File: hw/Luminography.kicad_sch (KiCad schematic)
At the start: 109 parts, among them J1 USB_C_Receptacle_PowerOnly_6P, J2 Conn_01x04, Q1 MMBT3904, Q2 2N7002, SW1 SW_Push, U1 LTC4054ES5-4.2, U100 BH1750FVI-TR, U101 BH1750FVI-TR, U102 BH1750FVI-TR, U103 BH1750FVI-TR, U104 BH1750FVI-TR, U105 BH1750FVI-TR, U106 BH1750FVI-TR, U107 BH1750FVI-TR, U108 BH1750FVI-TR, U109 BH1750FVI-TR, U110 BH1750FVI-TR, U111 BH1750FVI-TR, U112 BH1750FVI-TR, U113 BH1750FVI-TR, U114 BH1750FVI-TR, U115 BH1750FVI-TR, U116 BH1750FVI-TR, U117 BH1750FVI-TR, U118 BH1750FVI-TR, U119 BH1750FVI-TR, U120 BH1750FVI-TR, U121 BH1750FVI-TR, U122 BH1750FVI-TR, U123 BH1750FVI-TR, U2 XS3A1T3157GMX, U3 SPX3819M5-L-3-3, U4 MAX17048G+T10, U5 STM32G030K6Tx, U6 ZJY128R-IG01, U7 BMI270, U8 MMC5603NJ, U9 MAX98357AETE+, X1 12.288MHz

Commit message: Finish sensor array layout
そんなこと今更叶わない
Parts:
- C1, C10, C100, C101, C102, C103, C104, C105, C106, C107, C108, C109, C11, C110, C111, C112, C113, C114, C115, C116, C117, C118, C119, C12, C120, C121, C122, C123, C13, C14, C15, C2, C3, C4, C5, C6, C7, C8, C9: footprint Resistor_SMD:R_0402_1005Metric -> Capacitor_SMD:C_0402_1005Metric
- D1: footprint Resistor_SMD:R_0402_1005Metric -> Diode_SMD:D_SMB
- D2, D3: footprint Resistor_SMD:R_0402_1005Metric -> LED_SMD:LED_0603_1608Metric
- J1: footprint Resistor_SMD:R_0402_1005Metric -> Luminography_footprints:USB_C_Receptacle
- J2: footprint Resistor_SMD:R_0402_1005Metric -> Luminography_footprints:TestPoints_1x04_P2.0
- L1: footprint Resistor_SMD:R_0402_1005Metric -> Inductor_SMD:L_0402_1005Metric
- LS1: footprint Resistor_SMD:R_0402_1005Metric -> Luminography_footprints:Pads_1x02_P2.5
- Q1, Q2: footprint Resistor_SMD:R_0402_1005Metric -> Package_TO_SOT_SMD:SOT-23
- renumbered R101 to R102, R102 to R104, R103 to R106, R104 to R108, R105 to R110, R106 to R112, R107 to R114, R108 to R116, R109 to R118, R110 to R120, R111 to R122

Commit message: 🚧 Layout WIP
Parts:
- removed D3: White, LED_SMD:LED_0603_1608Metric, symbol Device:LED
- removed R13: 7.5k, Resistor_SMD:R_0402_1005Metric, symbol Device:R
- added C11: 100n, Capacitor_SMD:C_0402_1005Metric, symbol Device:C
- added U7: W25Q16JVUXIQ, W25Q16JVUXIQ:SON50P300X200X60-9N, symbol W25Q16JVUXIQ:W25Q16JVUXIQ
- renumbered C15 to C10, C9 to C12, C10 to C13, C11 to C14, C12 to C15, C13 to C16, C14 to C9, U9 to U10, U7 to U8, U8 to U9
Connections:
- net ACT_LED is gone; now on net I2Cx_SCL: U5.21 (PA10/NC)
- net GND: now also C11.1, U7.4 (GND), U7.9 (EP)
- net I2Cx_SCL: no longer U5.19 (PA9/NC)
- net PWR_LATCH: now also U5.22 (PA11/PA9)
- net SPI_MOSI: now also U7.5 (DI_(IO0))
- net SPI_SCK: now also U7.6 (CLK)
- net VDD: now also C11.2, U7.8 (VCC)
- net FLASH_CS: now reaches U5.20 (PC6)
- net FLASH_CS: now also U7.1 (~{CS})
- net BTN_INTR renamed BTNA_INTR
- new net SPI_MISO: U5.19 (PA9/NC), U7.2 (DO_(IO1))
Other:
- note added: "PA9 AF4 SPI2_MISO"
- moved on the sheet: R11

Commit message: 🚧 Routing WIP
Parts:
- removed Q1: MMBT3904, Package_TO_SOT_SMD:SOT-23, symbol Transistor_BJT:MMBT3904
- removed R5: 1M, Resistor_SMD:R_0402_1005Metric, symbol Device:R
- added R12: 1k, Resistor_SMD:R_0402_1005Metric, symbol Device:R
- added R6: 1M, Resistor_SMD:R_0402_1005Metric, symbol Device:R
- added SW2: SW_Push, Button_Switch_SMD:SW_SPST_TL3342, symbol Switch:SW_Push
- R5: renamed from R6; value 30k -> 1M
- renumbered Q2 to Q1, R12 to R13
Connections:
- net BTNA_INTR: now also R5.1, SW1.2, U2.3 (Y1), U5.22 (PA11/PA9); no longer R5.2
- net GND: now also R5.2, U8.1 (SDO), R6.2
- net I2Cx_SCL: now also U8.13 (SCX)
- net I2Cx_SDA_00: now also U8.14 (SDX)
- net LCD_CS: now also U5.1 (PB9); no longer U5.30 (PB6)
- net LCD_RSTN: now also U5.30 (PB6); no longer U5.1 (PB9)
- net PWR_LATCH: now also U5.3 (PC15); no longer U5.22 (PA11/PA9)
- net SPI_MOSI: no longer U8.14 (SDX)
- net SPI_SCK: no longer U8.13 (SCX)
- net SWDIO: now also R12.2; no longer U5.24 (PA13)
- net VDD: now also U8.12 (CSB), SW2.1; no longer R5.1
- removed net BMI_CS: U5.3 (PC15), U8.12 (CSB)
- new net BTNB_INTR: R12.1, R6.1, SW2.2, U5.24 (PA13)
- no-connect marks 16 -> 15
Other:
- note added: "Do not press when connected to a debug probe"
- note added: "Requires 5 V tolerance"
- moved on the sheet: C10, C3, C4, R13, R5, U3

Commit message: Board design almost done, do later
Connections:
- net I2Cx_SDA_00: now also U5.14 (PA7); no longer U5.7 (PA0)
- net I2Cx_SDA_01: now also U5.15 (PB0); no longer U5.8 (PA1)
- net I2Cx_SDA_02: now also U5.16 (PB1); no longer U5.9 (PA2)
- net I2Cx_SDA_03: now also U5.17 (PB2); no longer U5.10 (PA3)
- net I2Cx_SDA_04: now also U5.18 (PA8); no longer U5.11 (PA4)
- net I2Cx_SDA_05: now also U5.7 (PA0); no longer U5.12 (PA5)
- net I2Cx_SDA_06: now also U5.8 (PA1); no longer U5.13 (PA6)
- net I2Cx_SDA_07: now also U5.9 (PA2); no longer U5.14 (PA7)
- net I2Cx_SDA_08: now also U5.10 (PA3); no longer U5.15 (PB0)
- net I2Cx_SDA_09: now also U5.11 (PA4); no longer U5.16 (PB1)
- net I2Cx_SDA_10: now also U5.12 (PA5); no longer U5.17 (PB2)
- net I2Cx_SDA_11: now also U5.13 (PA6); no longer U5.18 (PA8)
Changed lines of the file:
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@@
     )
   )
-  (global_label "I2Cx_SDA_02" (shape bidirectional) (at 100.33 88.9 0) (fields_autoplaced)
+  (global_label "I2Cx_SDA_07" (shape bidirectional) (at 100.33 88.9 0) (fields_autoplaced)
     (effects (font (size 1.27 1.27)) (justify left))
     (property "Intersheetrefs" "${INTERSHEET_REFS}" (at 116.4612 88.9 0)
@@
     )
   )
-  (global_label "I2Cx_SDA_07" (shape bidirectional) (at 100.33 101.6 0) (fields_autoplaced)
+  (global_label "I2Cx_SDA_00" (shape bidirectional) (at 100.33 101.6 0) (fields_autoplaced)
     (effects (font (size 1.27 1.27)) (justify left))
     (property "Intersheetrefs" "${INTERSHEET_REFS}" (at 116.4612 101.6 0)
@@
     )
   )
-  (global_label "I2Cx_SDA_03" (shape bidirectional) (at 100.33 91.44 0) (fields_autoplaced)
+  (global_label "I2Cx_SDA_08" (shape bidirectional) (at 100.33 91.44 0) (fields_autoplaced)
     (effects (font (size 1.27 1.27)) (justify left))
     (property "Intersheetrefs" "${INTERSHEET_REFS}" (at 116.4612 91.44 0)
@@
     )
   )
-  (global_label "I2Cx_SDA_08" (shape bidirectional) (at 72.39 99.06 180) (fields_autoplaced)
+  (global_label "I2Cx_SDA_01" (shape bidirectional) (at 72.39 99.06 180) (fields_autoplaced)
     (effects (font (size 1.27 1.27)) (justify right))
     (property "Intersheetrefs" "${INTERSHEET_REFS}" (at 56.2588 99.06 0)
@@
     )
   )
-  (global_label "I2Cx_SDA_10" (shape bidirectional) (at 72.39 104.14 180) (fields_autoplaced)
+  (global_label "I2Cx_SDA_03" (shape bidirectional) (at 72.39 104.14 180) (fields_autoplaced)
     (effects (font (size 1.27 1.27)) (justify right))
     (property "Intersheetrefs" "${INTERSHEET_REFS}" (at 56.2588 104.14 0)
@@
     )
   )
-  (global_label "I2Cx_SDA_04" (shape bidirectional) (at 100.33 93.98 0) (fields_autoplaced)
+  (global_label "I2Cx_SDA_09" (shape bidirectional) (at 100.33 93.98 0) (fields_autoplaced)
     (effects (font (size 1.27 1.27)) (justify left))
     (property "Intersheetrefs" "${INTERSHEET_REFS}" (at 116.4612 93.98 0)
@@
     )
   )
-  (global_label "I2Cx_SDA_01" (shape bidirectional) (at 100.33 86.36 0) (fields_autoplaced)
+  (global_label "I2Cx_SDA_06" (shape bidirectional) (at 100.33 86.36 0) (fields_autoplaced)
     (effects (font (size 1.27 1.27)) (justify left))
     (property "Intersheetrefs" "${INTERSHEET_REFS}" (at 116.4612 86.36 0)
@@
     )
   )
-  (global_label "I2Cx_SDA_11" (shape bidirectional) (at 100.33 104.14 0) (fields_autoplaced)
+  (global_label "I2Cx_SDA_04" (shape bidirectional) (at 100.33 104.14 0) (fields_autoplaced)
     (effects (font (size 1.27 1.27)) (justify left))
     (property "Intersheetrefs" "${INTERSHEET_REFS}" (at 116.4612 104.14 0)
@@
     )
   )
-  (global_label "I2Cx_SDA_00" (shape bidirectional) (at 100.33 83.82 0) (fields_autoplaced)
+  (global_label "I2Cx_SDA_05" (shape bidirectional) (at 100.33 83.82 0) (fields_autoplaced)
     (effects (font (size 1.27 1.27)) (justify left))
     (property "Intersheetrefs" "${INTERSHEET_REFS}" (at 116.4612 83.82 0)
@@
     )
   )
-  (global_label "I2Cx_SDA_09" (shape bidirectional) (at 72.39 101.6 180) (fields_autoplaced)
+  (global_label "I2Cx_SDA_02" (shape bidirectional) (at 72.39 101.6 180) (fields_autoplaced)
     (effects (font (size 1.27 1.27)) (justify right))
     (property "Intersheetrefs" "${INTERSHEET_REFS}" (at 56.2588 101.6 0)
@@
     )
   )
-  (global_label "I2Cx_SDA_06" (shape bidirectional) (at 100.33 99.06 0) (fields_autoplaced)
+  (global_label "I2Cx_SDA_11" (shape bidirectional) (at 100.33 99.06 0) (fields_autoplaced)
     (effects (font (size 1.27 1.27)) (justify left))
     (property "Intersheetrefs" "${INTERSHEET_REFS}" (at 116.4612 99.06 0)
@@
     )
   )
-  (global_label "I2Cx_SDA_05" (shape bidirectional) (at 100.33 96.52 0) (fields_autoplaced)
+  (global_label "I2Cx_SDA_10" (shape bidirectional) (at 100.33 96.52 0) (fields_autoplaced)
     (effects (font (size 1.27 1.27)) (justify left))
     (property "Intersheetrefs" "${INTERSHEET_REFS}" (at 116.4612 96.52 0)

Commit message: Finish routing
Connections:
- net I2Cx_SDA_00: no longer U4.8 (SDA), U8.14 (SDX)
- net I2Cx_SDA_04: now also U8.14 (SDX)
- net I2Cx_SDA_06: now also U4.8 (SDA)
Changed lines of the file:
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@@
     )
   )
-  (global_label "I2Cx_SDA_00" (shape bidirectional) (at 335.28 31.115 0) (fields_autoplaced)
+  (global_label "I2Cx_SDA_06" (shape bidirectional) (at 335.28 31.115 0) (fields_autoplaced)
     (effects (font (size 1.27 1.27)) (justify left))
     (property "Intersheetrefs" "${INTERSHEET_REFS}" (at 351.4112 31.115 0)
@@
     )
   )
-  (global_label "I2Cx_SDA_00" (shape bidirectional) (at 151.765 149.86 90) (fields_autoplaced)
+  (global_label "I2Cx_SDA_04" (shape bidirectional) (at 151.765 149.86 90) (fields_autoplaced)
     (effects (font (size 1.27 1.27)) (justify left))
     (property "Intersheetrefs" "${INTERSHEET_REFS}" (at 151.765 133.7288 90)

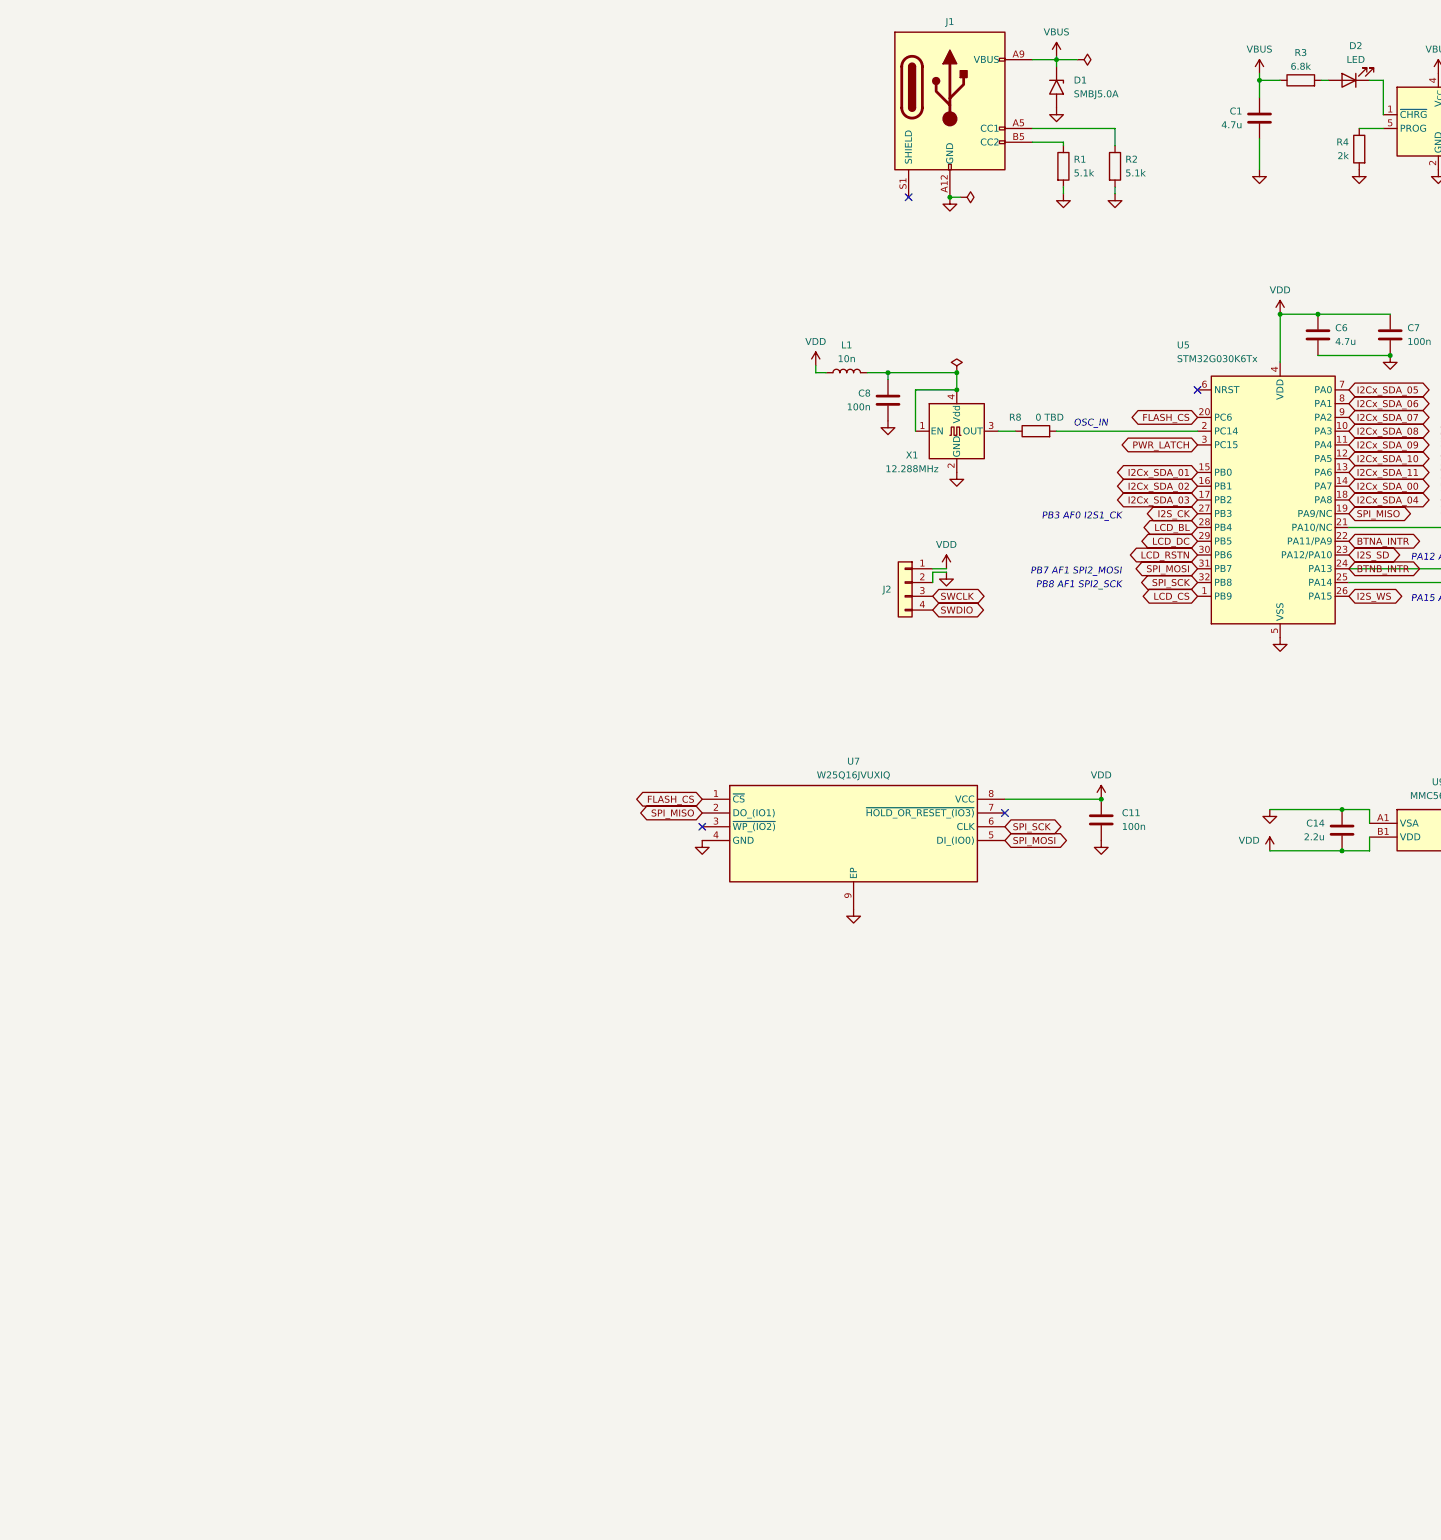
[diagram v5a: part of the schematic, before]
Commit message: 🚧 Add LEDs
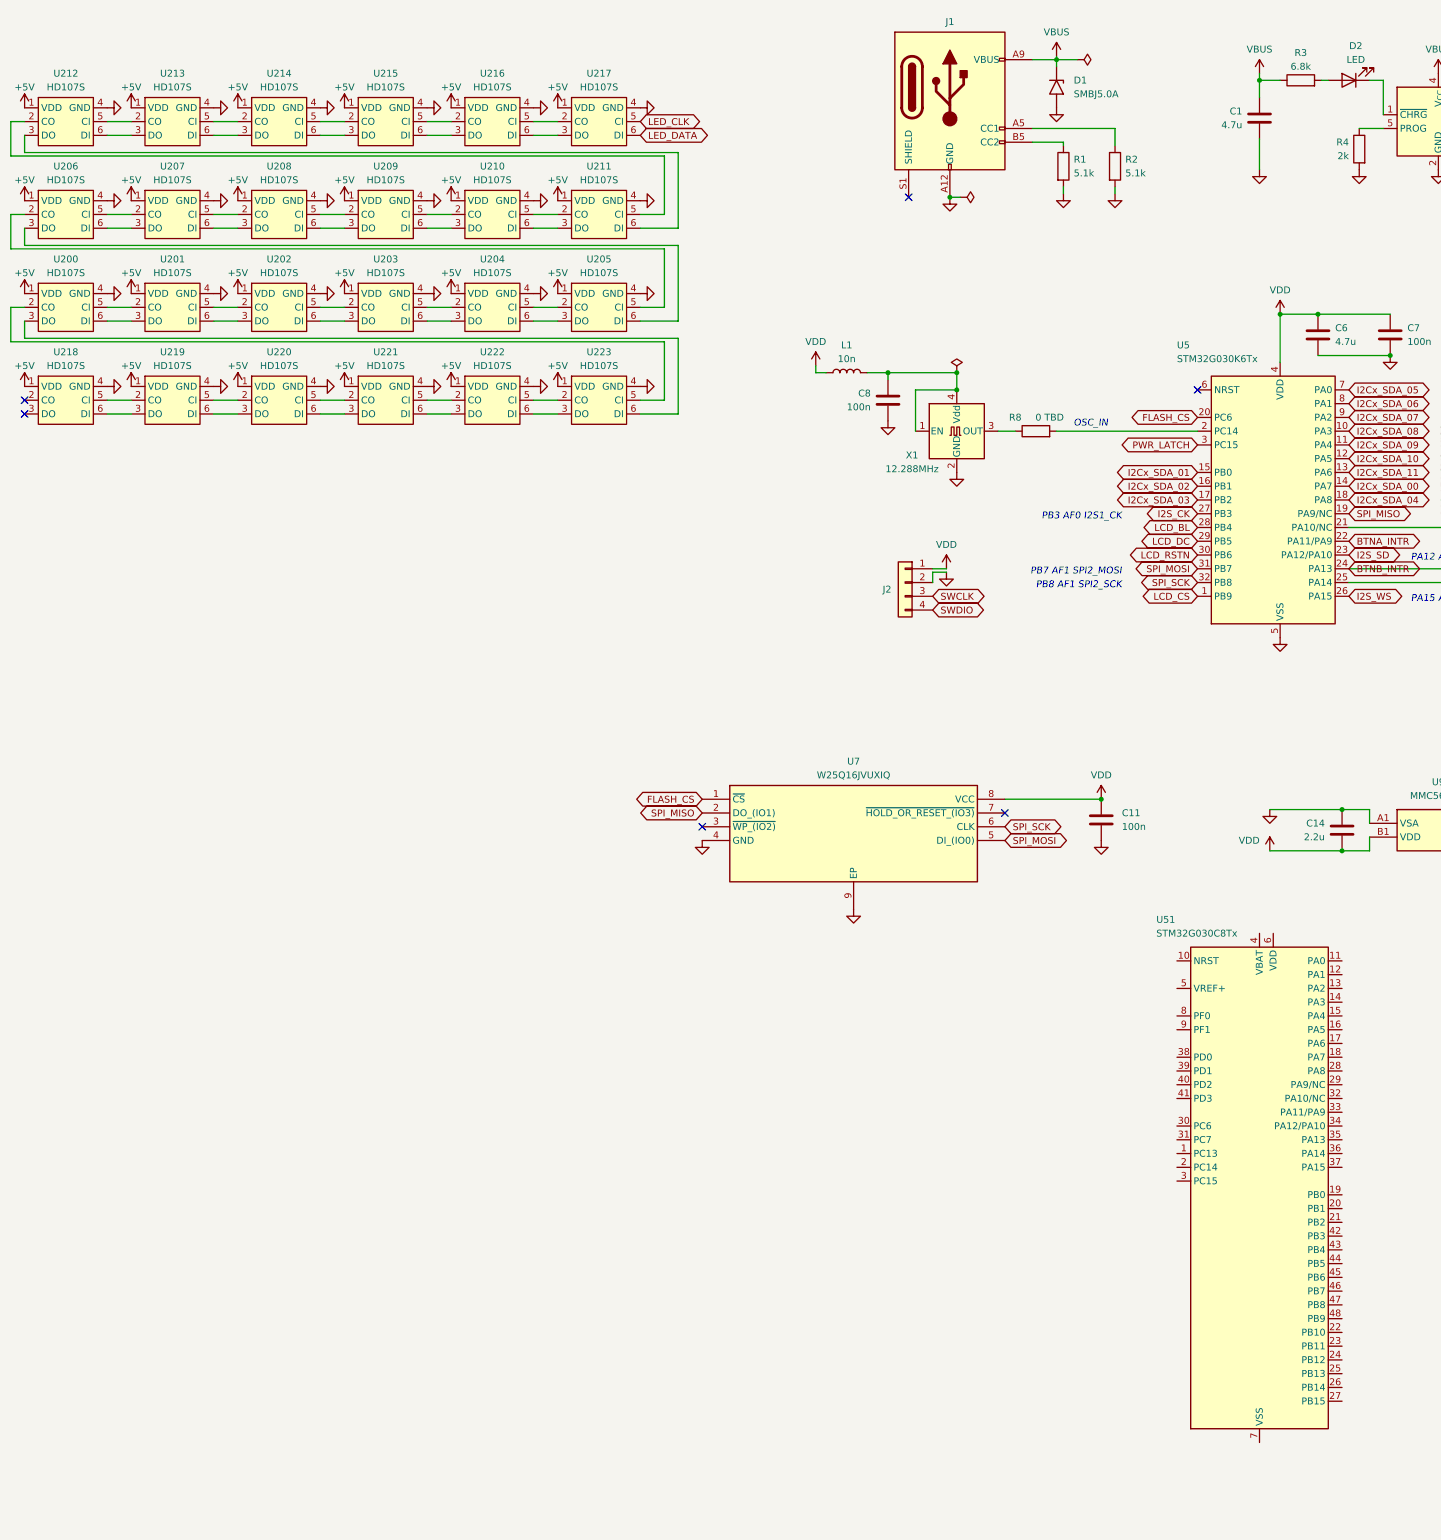
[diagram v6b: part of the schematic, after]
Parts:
- added U200, U201, U202, U203, U204, U205, U206, U207, U208, U209, U210, U211, U212, U213, U214, U215, U216, U217, U218, U219, U220, U221, U222, U223: HD107S, Luminography_footprints:HD107S_2020_6, symbol Luminography_symbols:HD107S
- added U51: STM32G030C8Tx, Package_QFP:LQFP-48_7x7mm_P0.5mm, symbol MCU_ST_STM32G0:STM32G030C8Tx
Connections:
- net GND: now also U200.4 (GND), U201.4 (GND), U202.4 (GND), U203.4 (GND), U204.4 (GND), U205.4 (GND), U206.4 (GND), U207.4 (GND), U208.4 (GND), U209.4 (GND), U210.4 (GND), U211.4 (GND), U212.4 (GND), U213.4 (GND), U214.4 (GND), U215.4 (GND), U216.4 (GND), U217.4 (GND), U218.4 (GND), U219.4 (GND), U220.4 (GND), U221.4 (GND), U222.4 (GND), U223.4 (GND)
- new net: U200.2 (CO), U223.5 (CI)
- new net: U200.3 (DO), U223.6 (DI)
- new net: U200.5 (CI), U201.2 (CO)
- new net: U200.6 (DI), U201.3 (DO)
- new net: U201.5 (CI), U202.2 (CO)
- new net: U201.6 (DI), U202.3 (DO)
- new net: U202.5 (CI), U203.2 (CO)
- new net: U202.6 (DI), U203.3 (DO)
- new net: U210.5 (CI), U211.2 (CO)
- new net: U210.6 (DI), U211.3 (DO)
- new net: U211.5 (CI), U212.2 (CO)
- new net: U211.6 (DI), U212.3 (DO)
- new net: U219.5 (CI), U220.2 (CO)
- new net: U219.6 (DI), U220.3 (DO)
- new net: U220.5 (CI), U221.2 (CO)
- new net: U220.6 (DI), U221.3 (DO)
- new net: U207.5 (CI), U208.2 (CO)
- new net: U207.6 (DI), U208.3 (DO)
- new net: U208.5 (CI), U209.2 (CO)
- new net: U208.6 (DI), U209.3 (DO)
- new net: U204.5 (CI), U205.2 (CO)
- new net: U204.6 (DI), U205.3 (DO)
- new net: U205.5 (CI), U206.2 (CO)
- new net: U205.6 (DI), U206.3 (DO)
- new net: U215.5 (CI), U216.2 (CO)
- new net: U215.6 (DI), U216.3 (DO)
- new net: U216.5 (CI), U217.2 (CO)
- new net: U216.6 (DI), U217.3 (DO)
- new net: U212.5 (CI), U213.2 (CO)
- new net: U212.6 (DI), U213.3 (DO)
- new net: U213.5 (CI), U214.2 (CO)
- new net: U213.6 (DI), U214.3 (DO)
- new net: U222.5 (CI), U223.2 (CO)
- new net: U222.6 (DI), U223.3 (DO)
- new net: U221.5 (CI), U222.2 (CO)
- new net: U221.6 (DI), U222.3 (DO)
- new net: U203.5 (CI), U204.2 (CO)
- new net: U203.6 (DI), U204.3 (DO)
- new net: U209.5 (CI), U210.2 (CO)
- new net: U209.6 (DI), U210.3 (DO)
- new net: U214.5 (CI), U215.2 (CO)
- new net: U214.6 (DI), U215.3 (DO)
- new net: U218.5 (CI), U219.2 (CO)
- new net: U218.6 (DI), U219.3 (DO)
- new net: U206.5 (CI), U207.2 (CO)
- new net: U206.6 (DI), U207.3 (DO)
- new net +5V: U200.1 (VDD), U201.1 (VDD), U202.1 (VDD), U203.1 (VDD), U204.1 (VDD), U205.1 (VDD), U206.1 (VDD), U207.1 (VDD), U208.1 (VDD), U209.1 (VDD), U210.1 (VDD), U211.1 (VDD), U212.1 (VDD), U213.1 (VDD), U214.1 (VDD), U215.1 (VDD), U216.1 (VDD), U217.1 (VDD), U218.1 (VDD), U219.1 (VDD), U220.1 (VDD), U221.1 (VDD), U222.1 (VDD), U223.1 (VDD)
- new net LED_CLK: U217.5 (CI)
- new net LED_DATA: U217.6 (DI)
- no-connect marks 15 -> 17

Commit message: Sleep
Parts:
- removed C8: 100n, Capacitor_SMD:C_0402_1005Metric, symbol Device:C
- removed L1: 10n, Inductor_SMD:L_0402_1005Metric, symbol Device:L
- removed R8: 0 TBD, Resistor_SMD:R_0402_1005Metric, symbol Device:R
- removed X1: 12.288MHz, Oscillator:Oscillator_SMD_Abracon_ASE-4Pin_3.2x2.5mm, symbol Oscillator:ASE-xxxMHz
- renumbered U51 to U5, U5 to U51
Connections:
- net GND: now also U5.7 (VSS); no longer U51.5 (VSS)
- net SWCLK: now also U5.36 (PA14); no longer U51.25 (PA14)
- net SWDIO: now also U5.35 (PA13); no longer R12.2
- net VDD: now also U5.4 (VBAT), U5.6 (VDD); no longer U51.4 (VDD)
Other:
- note removed: "Do not press when connected to a debug probe"
- note removed: "OSC_IN"
- moved on the sheet: C6, C7, U5
